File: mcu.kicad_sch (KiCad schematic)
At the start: 6 parts, among them J2 Conn_ARM_JTAG_SWD_10, J3 Conn_01x03_Male, J4 Conn_01x02_Male, U3 STM32L011F4Px

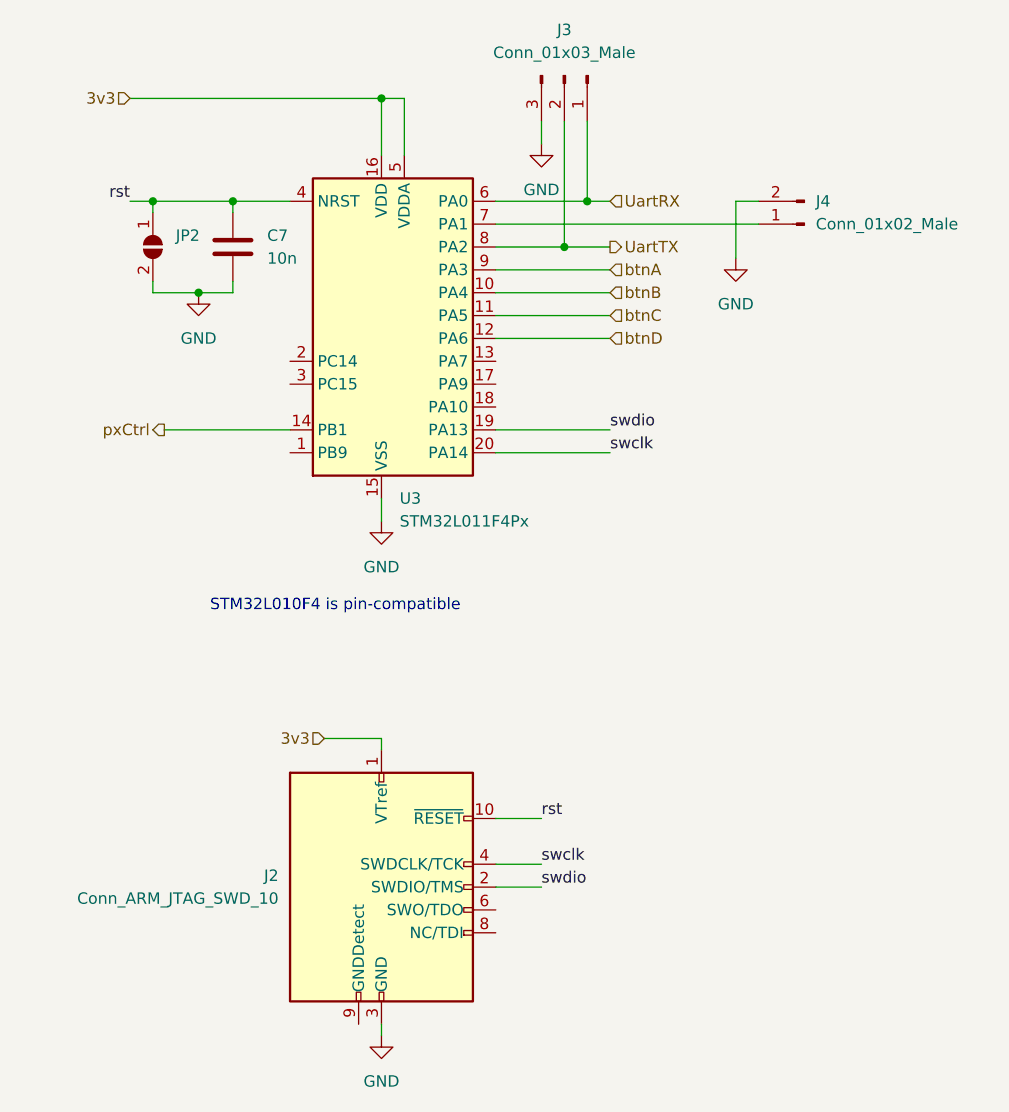
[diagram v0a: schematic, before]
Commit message: Swap FT231XQ for FT231XS
Signed-off-by: Giuseppe Barillari <joe2k01dev@gmail.com>
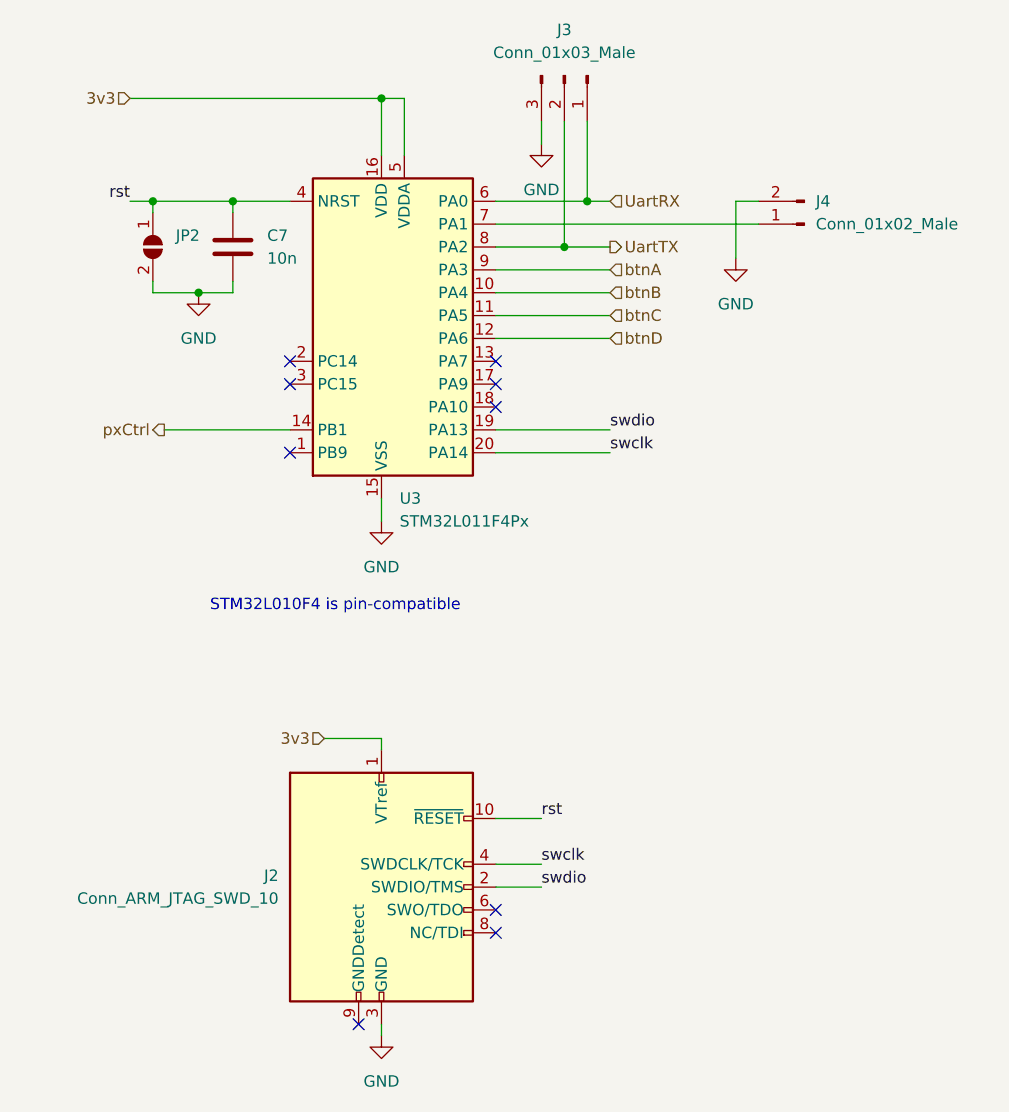
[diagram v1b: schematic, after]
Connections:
- no-connect marks 0 -> 9
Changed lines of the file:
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@@
   (junction (at 101.6 58.42) (diameter 0) (color 0 0 0 0)
   )
+  (no_connect (at 91.44 137.16))
+  (no_connect (at 91.44 139.7))
+  (no_connect (at 76.2 149.86))
+  (no_connect (at 68.58 76.2))
+  (no_connect (at 68.58 78.74))
+  (no_connect (at 91.44 76.2))
+  (no_connect (at 91.44 78.74))
+  (no_connect (at 91.44 81.28))
+  (no_connect (at 68.58 86.36))
   (wire (pts (xy 78.74 91.44) (xy 78.74 93.98))
     (stroke (width 0) (type default) (color 0 0 0 0))

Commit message: Start laying out pcb
Signed-off-by: Giuseppe Barillari <joe2k01dev@gmail.com>
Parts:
- added R4: 10k, Resistor_SMD:R_0805_2012Metric_Pad1.20x1.40mm_HandSolder, symbol Device:R
- added SW2: SW_Push, Button_Switch_SMD:SW_Push_1P1T_NO_6x6mm_H9.5mm, symbol Switch:SW_Push
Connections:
- net GND: now also R4.2
- net at U3.1 (PB9): now also R4.1, SW2.2
- net btnB: no longer names the net of U3.10 (PA4)
- net btnC: no longer names the net of U3.11 (PA5)
- net btnD: no longer names the net of U3.12 (PA6)
- new net +3.3V: SW2.1
- no-connect marks 9 -> 11
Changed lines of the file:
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@@
   (junction (at 78.74 46.99) (diameter 0) (color 0 0 0 0)
   )
+  (junction (at 71.12 99.06) (diameter 0) (color 0 0 0 0)
+  )
   (junction (at 62.23 58.42) (diameter 0) (color 0 0 0 0)
   )
@@
   (junction (at 101.6 58.42) (diameter 0) (color 0 0 0 0)
   )
+  (junction (at 64.77 86.36) (diameter 0) (color 0 0 0 0)
+  )
+  (no_connect (at 91.44 68.58))
+  (no_connect (at 91.44 71.12))
+  (no_connect (at 91.44 73.66))
   (no_connect (at 91.44 137.16))
   (no_connect (at 91.44 139.7))
@@
   (no_connect (at 91.44 78.74))
   (no_connect (at 91.44 81.28))
-  (no_connect (at 68.58 86.36))
-  (wire (pts (xy 78.74 91.44) (xy 78.74 93.98))
-    (stroke (width 0) (type default) (color 0 0 0 0))
-  )
   (wire (pts (xy 91.44 60.96) (xy 120.65 60.96))
     (stroke (width 0) (type default) (color 0 0 0 0))
   )
+  (wire (pts (xy 60.96 86.36) (xy 64.77 86.36))
+    (stroke (width 0) (type default) (color 0 0 0 0))
+  )
   (wire (pts (xy 78.74 46.99) (xy 50.8 46.99))
     (stroke (width 0) (type default) (color 0 0 0 0))
@@
     (stroke (width 0) (type default) (color 0 0 0 0))
   )
+  (wire (pts (xy 78.74 91.44) (xy 78.74 99.06))
+    (stroke (width 0) (type default) (color 0 0 0 0))
+  )
+  (wire (pts (xy 71.12 99.06) (xy 71.12 100.33))
+    (stroke (width 0) (type default) (color 0 0 0 0))
+  )
   (wire (pts (xy 91.44 83.82) (xy 104.14 83.82))
     (stroke (width 0) (type default) (color 0 0 0 0))
   )
+  (wire (pts (xy 41.91 86.36) (xy 50.8 86.36))
+    (stroke (width 0) (type default) (color 0 0 0 0))
+  )
   (wire (pts (xy 81.28 53.34) (xy 81.28 46.99))
     (stroke (width 0) (type default) (color 0 0 0 0))
@@
     (stroke (width 0) (type default) (color 0 0 0 0))
   )
+  (wire (pts (xy 64.77 86.36) (xy 68.58 86.36))
+    (stroke (width 0) (type default) (color 0 0 0 0))
+  )
+  (wire (pts (xy 68.58 83.82) (xy 66.04 83.82))
+    (stroke (width 0) (type default) (color 0 0 0 0))
+  )
   (wire (pts (xy 99.06 63.5) (xy 104.14 63.5))
     (stroke (width 0) (type default) (color 0 0 0 0))
@@
     (stroke (width 0) (type default) (color 0 0 0 0))
   )
+  (wire (pts (xy 64.77 96.52) (xy 64.77 99.06))
+    (stroke (width 0) (type default) (color 0 0 0 0))
+  )
+  (wire (pts (xy 78.74 99.06) (xy 71.12 99.06))
+    (stroke (width 0) (type default) (color 0 0 0 0))
+  )
   (wire (pts (xy 101.6 49.53) (xy 101.6 58.42))
     (stroke (width 0) (type default) (color 0 0 0 0))
   )
-  (wire (pts (xy 91.44 71.12) (xy 104.14 71.12))
-    (stroke (width 0) (type default) (color 0 0 0 0))
-  )
   (wire (pts (xy 58.42 68.58) (xy 62.23 68.58))
     (stroke (width 0) (type default) (color 0 0 0 0))
   )
-  (wire (pts (xy 54.61 83.82) (xy 68.58 83.82))
+  (wire (pts (xy 66.04 78.74) (xy 54.61 78.74))
+    (stroke (width 0) (type default) (color 0 0 0 0))
+  )
+  (wire (pts (xy 64.77 99.06) (xy 71.12 99.06))
+    (stroke (width 0) (type default) (color 0 0 0 0))
+  )
+  (wire (pts (xy 66.04 83.82) (xy 66.04 78.74))
     (stroke (width 0) (type default) (color 0 0 0 0))
   )
@@
     (stroke (width 0) (type default) (color 0 0 0 0))
   )
+  (wire (pts (xy 64.77 86.36) (xy 64.77 88.9))
+    (stroke (width 0) (type default) (color 0 0 0 0))
+  )
   (wire (pts (xy 53.34 58.42) (xy 53.34 59.69))
     (stroke (width 0) (type default) (color 0 0 0 0))
@@
     (stroke (width 0) (type default) (color 0 0 0 0))
   )
-  (wire (pts (xy 91.44 68.58) (xy 104.14 68.58))
-    (stroke (width 0) (type default) (color 0 0 0 0))
-  )
   (wire (pts (xy 118.11 58.42) (xy 120.65 58.42))
     (stroke (width 0) (type default) (color 0 0 0 0))
@@
     (stroke (width 0) (type default) (color 0 0 0 0))
   )
-  (wire (pts (xy 91.44 73.66) (xy 104.14 73.66))
-    (stroke (width 0) (type default) (color 0 0 0 0))
-  )
   (wire (pts (xy 78.74 118.11) (xy 72.39 118.11))
     (stroke (width 0) (type default) (color 0 0 0 0))
   )
-  (text "STM32L010F4 is pin-compatible" (at 59.69 104.14 0)
+  (text "STM32L010F4 is pin-compatible" (at 52.07 43.18 0)
     (effects (font (size 1.27 1.27)) (justify left bottom))
   )
@@
     (effects (font (size 1.27 1.27)) (justify left bottom))
   )
-  (hierarchical_label "btnC" (shape input) (at 104.14 71.12 0)
-    (effects (font (size 1.27 1.27)) (justify left))
-  )
   (hierarchical_label "3v3" (shape input) (at 50.8 46.99 180)
     (effects (font (size 1.27 1.27)) (justify right))
@@
     (effects (font (size 1.27 1.27)) (justify left))
   )
-  (hierarchical_label "btnB" (shape input) (at 104.14 68.58 0)
-    (effects (font (size 1.27 1.27)) (justify left))
-  )
-  (hierarchical_label "btnD" (shape input) (at 104.14 73.66 0)
-    (effects (font (size 1.27 1.27)) (justify left))
-  )
-  (hierarchical_label "pxCtrl" (shape output) (at 54.61 83.82 180)
+  (hierarchical_label "pxCtrl" (shape output) (at 54.61 78.74 180)
     (effects (font (size 1.27 1.27)) (justify right))
   )
@@
     (pin "2")
     (pin "3")
+  )
+  (symbol (lib_id "Device:R") (at 64.77 92.71 0) (unit 1)
+    (in_bom yes) (on_board yes) (fields_autoplaced)
+    (property "Reference" "R4" (id 0) (at 67.31 91.4399 0)
+      (effects (font (size 1.27 1.27)) (justify left))
+    )
+    (property "Value" "10k" (id 1) (at 67.31 93.9799 0)
+      (effects (font (size 1.27 1.27)) (justify left))
+    )
+    (property "Footprint" "Resistor_SMD:R_0805_2012Metric_Pad1.20x1.40mm_HandSolder" (id 2) (at 62.992 92.71 90)
+      (effects (font (size 1.27 1.27)) hide)
+    )
+    (property "Datasheet" "~" (id 3) (at 64.77 92.71 0)
+      (effects (font (size 1.27 1.27)) hide)
+    )
+    (pin "1")
+    (pin "2")
   )
   (symbol (lib_id "power:GND") (at 78.74 151.13 0) (unit 1)
@@
     (pin "1")
   )
+  (symbol (lib_id "power:+3.3V") (at 41.91 86.36 0) (unit 1)
+    (in_bom yes) (on_board yes) (fields_autoplaced)
+    (property "Reference" "#PWR?" (id 0) (at 41.91 90.17 0)
+      (effects (font (size 1.27 1.27)) hide)
+    )
+    (property "Value" "+3.3V" (id 1) (at 41.91 81.28 0))
+    (property "Footprint" "" (id 2) (at 41.91 86.36 0)
+      (effects (font (size 1.27 1.27)) hide)
+    )
+    (property "Datasheet" "" (id 3) (at 41.91 86.36 0)
+      (effects (font (size 1.27 1.27)) hide)
+    )
+    (pin "1")
+  )
   (symbol (lib_id "Jumper:SolderJumper_2_Open") (at 53.34 63.5 270) (unit 1)
     (in_bom yes) (on_board yes)
@@
     (pin "2")
   )
+  (symbol (lib_id "Switch:SW_Push") (at 55.88 86.36 0) (unit 1)
+    (in_bom yes) (on_board yes)
+    (property "Reference" "SW2" (id 0) (at 55.88 88.9 0))
+    (property "Value" "SW_Push" (id 1) (at 55.88 91.44 0))
+    (property "Footprint" "Button_Switch_SMD:SW_Push_1P1T_NO_6x6mm_H9.5mm" (id 2) (at 55.88 81.28 0)
+      (effects (font (size 1.27 1.27)) hide)
+    )
+    (property "Datasheet" "~" (id 3) (at 55.88 81.28 0)
+      (effects (font (size 1.27 1.27)) hide)
+    )
+    (pin "1")
+    (pin "2")
+  )
   (symbol (lib_id "Device:C") (at 62.23 63.5 0) (unit 1)
     (in_bom yes) (on_board yes) (fields_autoplaced)
@@
     (pin "2")
   )
-  (symbol (lib_id "power:GND") (at 78.74 93.98 0) (unit 1)
-    (in_bom yes) (on_board yes) (fields_autoplaced)
-    (property "Reference" "#PWR022" (id 0) (at 78.74 100.33 0)
-      (effects (font (size 1.27 1.27)) hide)
-    )
-    (property "Value" "GND" (id 1) (at 78.74 99.06 0))
-    (property "Footprint" "" (id 2) (at 78.74 93.98 0)
-      (effects (font (size 1.27 1.27)) hide)
-    )
-    (property "Datasheet" "" (id 3) (at 78.74 93.98 0)
-      (effects (font (size 1.27 1.27)) hide)
-    )
+  (symbol (lib_id "power:GND") (at 71.12 100.33 0) (unit 1)
+    (in_bom yes) (on_board yes) (fields_autoplaced)
+    (property "Reference" "#PWR022" (id 0) (at 71.12 106.68 0)
+      (effects (font (size 1.27 1.27)) hide)
+    )
+    (property "Value" "GND" (id 1) (at 71.12 105.41 0))
+    (property "Footprint" "" (id 2) (at 71.12 100.33 0)
+      (effects (font (size 1.27 1.27)) hide)
+    )
+    (property "Datasheet" "" (id 3) (at 71.12 100.33 0)
+      (effects (font (size 1.27 1.27)) hide)
+    )
